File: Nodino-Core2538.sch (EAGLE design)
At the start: 20 parts, among them CON1 NODINO-JTAGMODULE, CON2 USB-OTG_SHIELD, IC1 CC2538, IC2 AP733333SAG, Q1 32MHz, Q2 32.768kHz

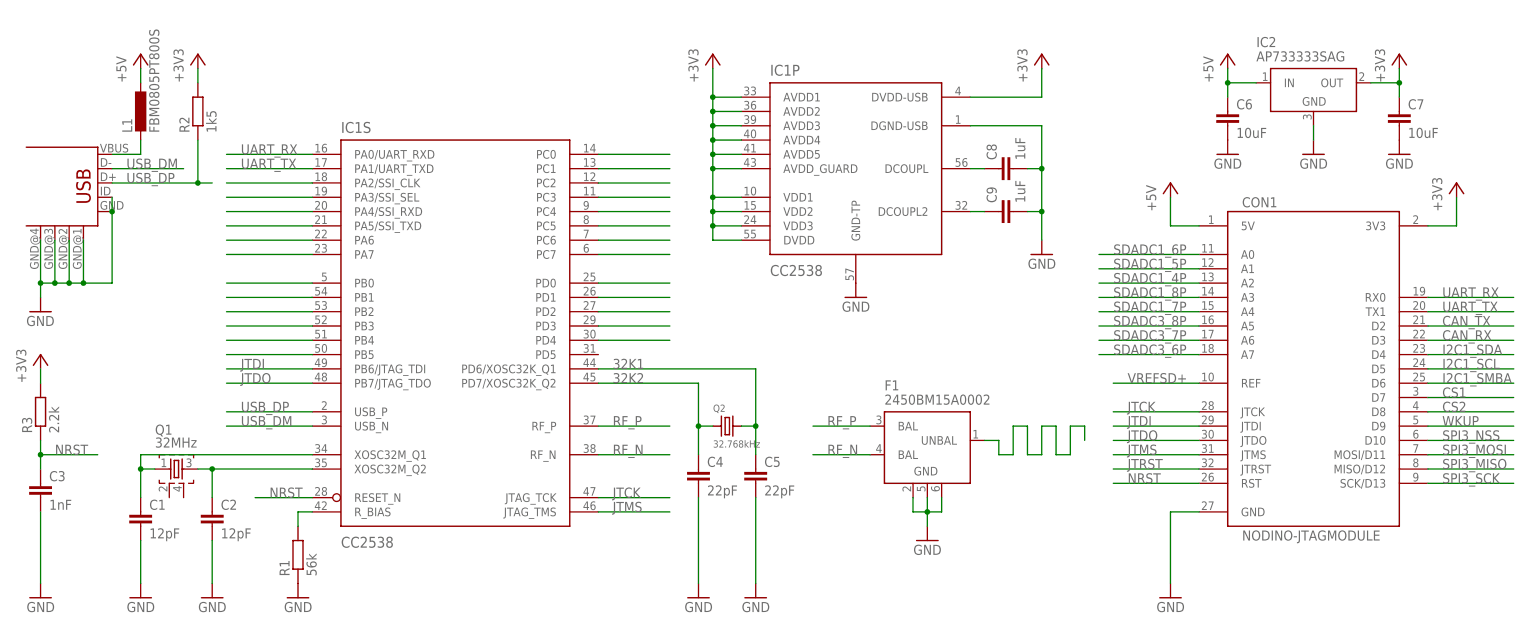
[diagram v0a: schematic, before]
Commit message: almost done, but I think we need to remove the chip antenna
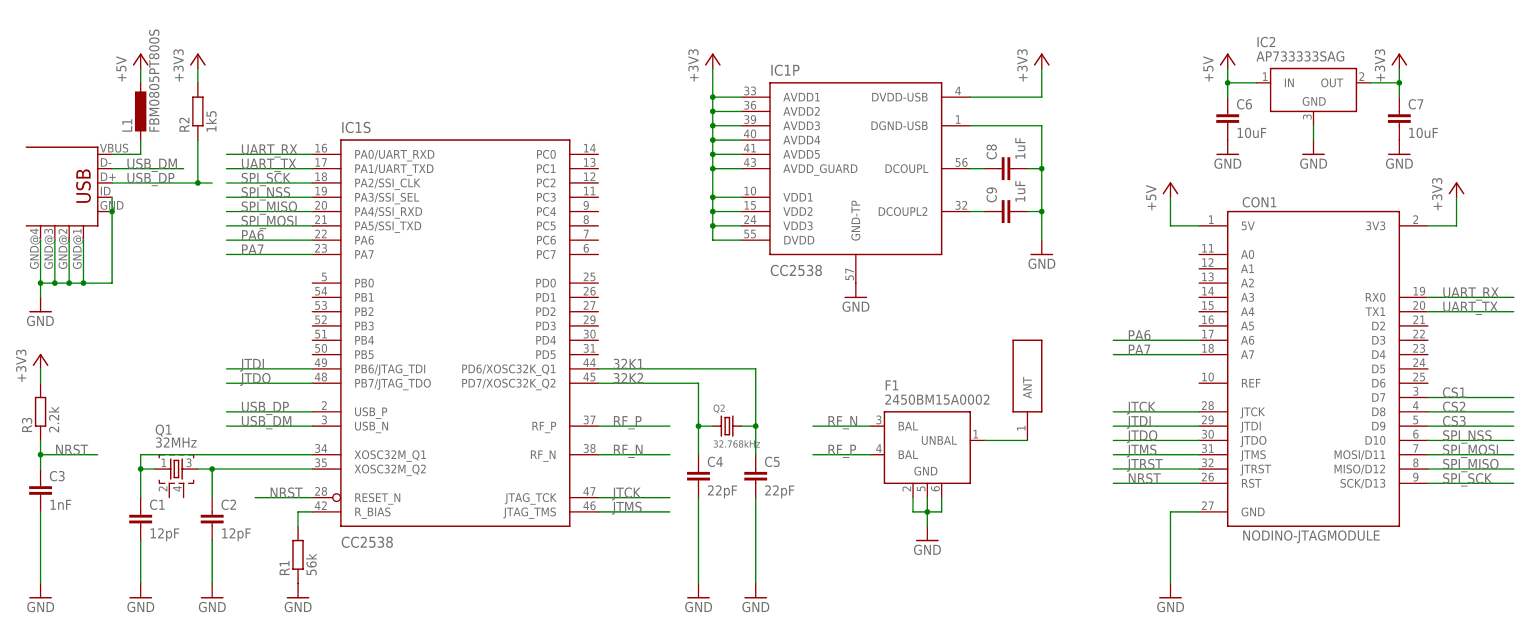
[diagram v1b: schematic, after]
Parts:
- added ANT1: 2450AT18B100, johanson-technology:2450AT18B100
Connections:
- net WKUP renamed CS3
- removed net CAN_RX: CON1.D3
- removed net CAN_TX: CON1.D2
- removed net I2C1_SCL: CON1.D5
- removed net I2C1_SDA: CON1.D4
- removed net I2C1_SMBA: CON1.D6
- removed net N$10: IC1S.PB3
- removed net N$11: IC1S.PB2
- removed net N$12: IC1S.PB1
- removed net N$13: IC1S.PB0
- removed net N$14: IC1S.PA7
- removed net N$15: IC1S.PA6
- removed net N$16: IC1S.PA5/SSI_TXD
- removed net N$17: IC1S.PA4/SSI_RXD
- removed net N$18: IC1S.PA3/SSI_SEL
- removed net N$19: IC1S.PA2/SSI_CLK
- removed net N$22: IC1S.PC0
- removed net N$23: IC1S.PC1
- removed net N$24: IC1S.PC2
- removed net N$25: IC1S.PC3
- removed net N$26: IC1S.PC4
- removed net N$27: IC1S.PC5
- removed net N$28: IC1S.PC6
- removed net N$29: IC1S.PC7
- removed net N$30: IC1S.PD0
- removed net N$31: IC1S.PD1
- removed net N$32: IC1S.PD2
- removed net N$33: IC1S.PD3
- removed net N$34: IC1S.PD4
- removed net N$6: IC1S.PB5
- removed net N$9: IC1S.PB4
- removed net SDADC1_4P: CON1.A2
- removed net SDADC1_5P: CON1.A1
- removed net SDADC1_6P: CON1.A0
- removed net SDADC1_7P: CON1.A4
- removed net SDADC1_8P: CON1.A3
- removed net SDADC3_6P: CON1.A7
- removed net SDADC3_7P: CON1.A6
- removed net SDADC3_8P: CON1.A5
- removed net SPI3_MISO: CON1.MISO/D12
- removed net SPI3_MOSI: CON1.MOSI/D11
- removed net SPI3_NSS: CON1.D10
- removed net SPI3_SCK: CON1.SCK/D13
- removed net VREFSD+: CON1.REF
- new net PA6: CON1.A6, IC1S.PA6
- new net PA7: CON1.A7, IC1S.PA7
- new net SPI_MISO: CON1.MISO/D12, IC1S.PA4/SSI_RXD
- new net SPI_MOSI: CON1.MOSI/D11, IC1S.PA5/SSI_TXD
- new net SPI_NSS: CON1.D10, IC1S.PA3/SSI_SEL
- new net SPI_SCK: CON1.SCK/D13, IC1S.PA2/SSI_CLK
- net N$2: now also ANT1.ANT
- net RF_N: now also F1.BAL@1; no longer F1.BAL@2
- net RF_P: now also F1.BAL@2; no longer F1.BAL@1

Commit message: added CS1, CS2, CS3
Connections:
- net CS1: now also IC1S.PC2
- net CS2: now also IC1S.PC1
- net CS3: now also IC1S.PC0
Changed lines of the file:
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@@
 <setting verticaltext="up"/>
 </settings>
-<grid distance="0.1" unitdist="inch" unit="inch" style="lines" multiple="1" display="no" altdistance="0.01" altunitdist="inch" altunit="inch"/>
+<grid distance="0.1" unitdist="inch" unit="inch" style="lines" multiple="1" display="yes" altdistance="0.01" altunitdist="inch" altunit="inch"/>
 <layers>
 <layer number="1" name="Top" color="4" fill="1" visible="no" active="no"/>
@@
 <label x="261.62" y="33.02" size="1.778" layer="95"/>
 </segment>
+<segment>
+<pinref part="IC1" gate="S" pin="PC1"/>
+<wire x1="121.92" y1="76.2" x2="111.76" y2="76.2" width="0.1524" layer="91"/>
+<label x="114.3" y="76.2" size="1.778" layer="95"/>
+</segment>
 </net>
 <net name="JTDO" class="0">
@@
 <wire x1="274.32" y1="35.56" x2="259.08" y2="35.56" width="0.1524" layer="91"/>
 <label x="261.62" y="35.56" size="1.778" layer="95"/>
+</segment>
+<segment>
+<pinref part="IC1" gate="S" pin="PC2"/>
+<wire x1="121.92" y1="73.66" x2="111.76" y2="73.66" width="0.1524" layer="91"/>
+<label x="114.3" y="73.66" size="1.778" layer="95"/>
 </segment>
 </net>
@@
 <label x="261.62" y="30.48" size="1.778" layer="95"/>
 </segment>
-</net>
+<segment>
+<pinref part="IC1" gate="S" pin="PC0"/>
+<wire x1="121.92" y1="78.74" x2="111.76" y2="78.74" width="0.1524" layer="91"/>
+<label x="114.3" y="78.74" size="1.778" layer="95"/>
+</segment>
+</net>

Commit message: added D2-D6
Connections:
- new net PB1: CON1.D6, IC1S.PB1
- new net PB2: CON1.D5, IC1S.PB2
- new net PB3: CON1.D4, IC1S.PB3
- new net PB4: CON1.D3, IC1S.PB4
- new net PB5: CON1.D2, IC1S.PB5
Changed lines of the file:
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@@
 <setting verticaltext="up"/>
 </settings>
-<grid distance="0.1" unitdist="inch" unit="inch" style="lines" multiple="1" display="yes" altdistance="0.01" altunitdist="inch" altunit="inch"/>
+<grid distance="0.1" unitdist="inch" unit="inch" style="lines" multiple="1" display="no" altdistance="0.01" altunitdist="inch" altunit="inch"/>
 <layers>
 <layer number="1" name="Top" color="4" fill="1" visible="no" active="no"/>
@@
 </segment>
 </net>
+<net name="PB4" class="0">
+<segment>
+<pinref part="IC1" gate="S" pin="PB4"/>
+<wire x1="45.72" y1="45.72" x2="60.96" y2="45.72" width="0.1524" layer="91"/>
+<label x="48.26" y="45.72" size="1.778" layer="95"/>
+</segment>
+<segment>
+<pinref part="CON1" gate="G$1" pin="D3"/>
+<wire x1="274.32" y1="45.72" x2="259.08" y2="45.72" width="0.1524" layer="91"/>
+<label x="261.62" y="45.72" size="1.778" layer="95"/>
+</segment>
+</net>
+<net name="PB3" class="0">
+<segment>
+<pinref part="IC1" gate="S" pin="PB3"/>
+<wire x1="45.72" y1="48.26" x2="60.96" y2="48.26" width="0.1524" layer="91"/>
+<label x="48.26" y="48.26" size="1.778" layer="95"/>
+</segment>
+<segment>
+<pinref part="CON1" gate="G$1" pin="D4"/>
+<wire x1="274.32" y1="43.18" x2="259.08" y2="43.18" width="0.1524" layer="91"/>
+<label x="261.62" y="43.18" size="1.778" layer="95"/>
+</segment>
+</net>
+<net name="PB2" class="0">
+<segment>
+<pinref part="IC1" gate="S" pin="PB2"/>
+<wire x1="45.72" y1="50.8" x2="60.96" y2="50.8" width="0.1524" layer="91"/>
+<label x="48.26" y="50.8" size="1.778" layer="95"/>
+</segment>
+<segment>
+<pinref part="CON1" gate="G$1" pin="D5"/>
+<wire x1="274.32" y1="40.64" x2="259.08" y2="40.64" width="0.1524" layer="91"/>
+<label x="261.62" y="40.64" size="1.778" layer="95"/>
+</segment>
+</net>
+<net name="PB1" class="0">
+<segment>
+<pinref part="IC1" gate="S" pin="PB1"/>
+<wire x1="45.72" y1="53.34" x2="60.96" y2="53.34" width="0.1524" layer="91"/>
+<label x="48.26" y="53.34" size="1.778" layer="95"/>
+</segment>
+<segment>
+<pinref part="CON1" gate="G$1" pin="D6"/>
+<wire x1="274.32" y1="38.1" x2="259.08" y2="38.1" width="0.1524" layer="91"/>
+<label x="261.62" y="38.1" size="1.778" layer="95"/>
+</segment>
+</net>
+<net name="PB5" class="0">
+<segment>
+<pinref part="IC1" gate="S" pin="PB5"/>
+<wire x1="45.72" y1="43.18" x2="60.96" y2="43.18" width="0.1524" layer="91"/>
+<label x="48.26" y="43.18" size="1.778" layer="95"/>
+</segment>
+<segment>
+<pinref part="CON1" gate="G$1" pin="D2"/>
+<wire x1="274.32" y1="48.26" x2="259.08" y2="48.26" width="0.1524" layer="91"/>
+<label x="261.62" y="48.26" size="1.778" layer="95"/>
+</segment>
+</net>

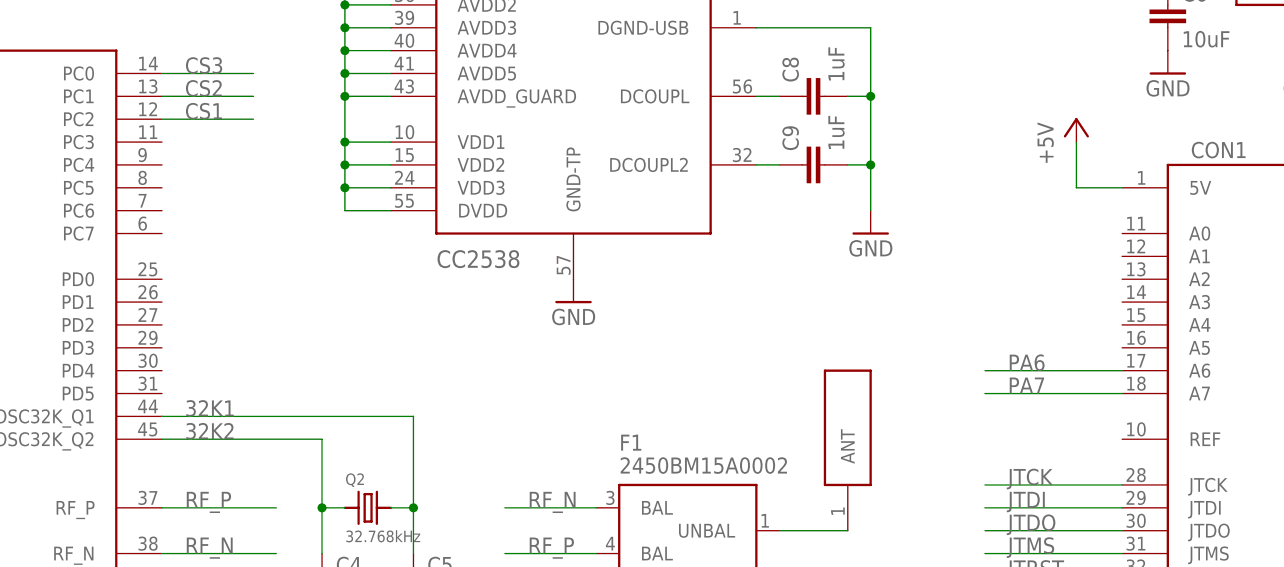
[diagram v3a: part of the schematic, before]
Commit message: added D15-D17
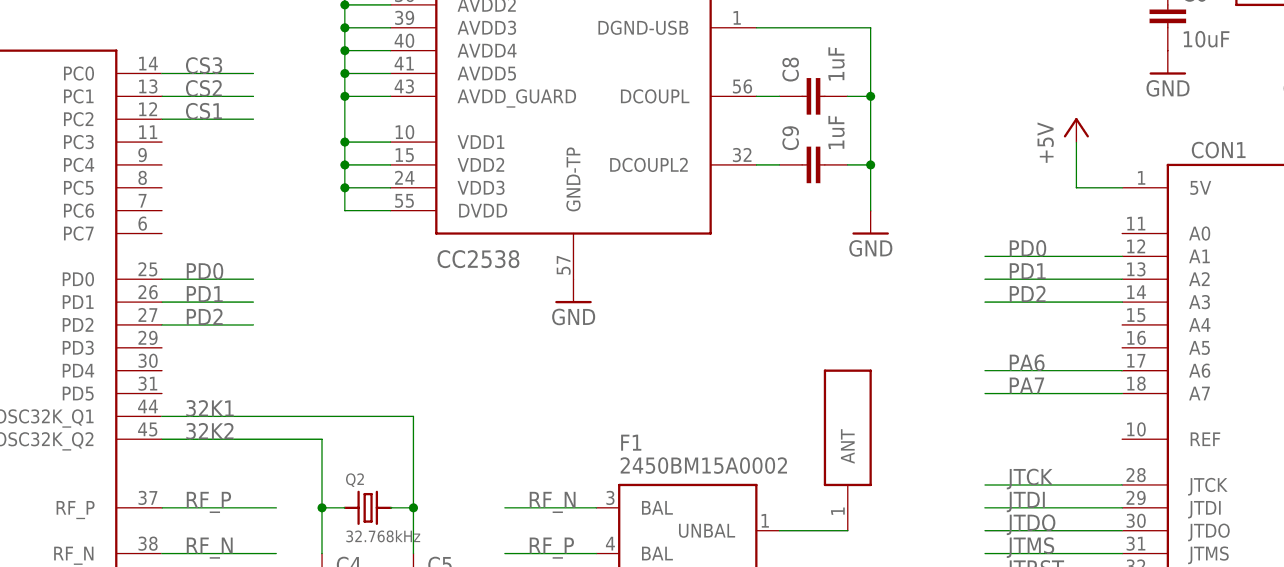
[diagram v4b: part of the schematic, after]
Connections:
- new net PD0: CON1.A1, IC1S.PD0
- new net PD1: CON1.A2, IC1S.PD1
- new net PD2: CON1.A3, IC1S.PD2
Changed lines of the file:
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@@
+</segment>
+</net>
+<net name="PD0" class="0">
+<segment>
+<pinref part="IC1" gate="S" pin="PD0"/>
+<wire x1="121.92" y1="55.88" x2="111.76" y2="55.88" width="0.1524" layer="91"/>
+<label x="114.3" y="55.88" size="1.778" layer="95"/>
+</segment>
+<segment>
+<pinref part="CON1" gate="G$1" pin="A1"/>
+<wire x1="203.2" y1="58.42" x2="218.44" y2="58.42" width="0.1524" layer="91"/>
+<label x="205.74" y="58.42" size="1.778" layer="95"/>
+</segment>
+</net>
+<net name="PD1" class="0">
+<segment>
+<pinref part="IC1" gate="S" pin="PD1"/>
+<wire x1="121.92" y1="53.34" x2="111.76" y2="53.34" width="0.1524" layer="91"/>
+<label x="114.3" y="53.34" size="1.778" layer="95"/>
+</segment>
+<segment>
+<pinref part="CON1" gate="G$1" pin="A2"/>
+<wire x1="203.2" y1="55.88" x2="218.44" y2="55.88" width="0.1524" layer="91"/>
+<label x="205.74" y="55.88" size="1.778" layer="95"/>
+</segment>
+</net>
+<net name="PD2" class="0">
+<segment>
+<pinref part="IC1" gate="S" pin="PD2"/>
+<wire x1="121.92" y1="50.8" x2="111.76" y2="50.8" width="0.1524" layer="91"/>
+<label x="114.3" y="50.8" size="1.778" layer="95"/>
+</segment>
+<segment>
+<pinref part="CON1" gate="G$1" pin="A3"/>
+<wire x1="203.2" y1="53.34" x2="218.44" y2="53.34" width="0.1524" layer="91"/>
+<label x="205.74" y="53.34" size="1.778" layer="95"/>
 </segment>
 </net>
